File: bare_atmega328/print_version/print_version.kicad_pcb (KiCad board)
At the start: 2 copper layers, 17 parts, among them J1 22-23-2021, J2 22-23-2021, J3 640456-3, J4 22-23-2021, J5 Conn_01x14_Male, J6 Conn_01x14_Male, J7 640456-3, SW1 SW_Push, U1 ATMEGA328-PU, Y1 Crystal

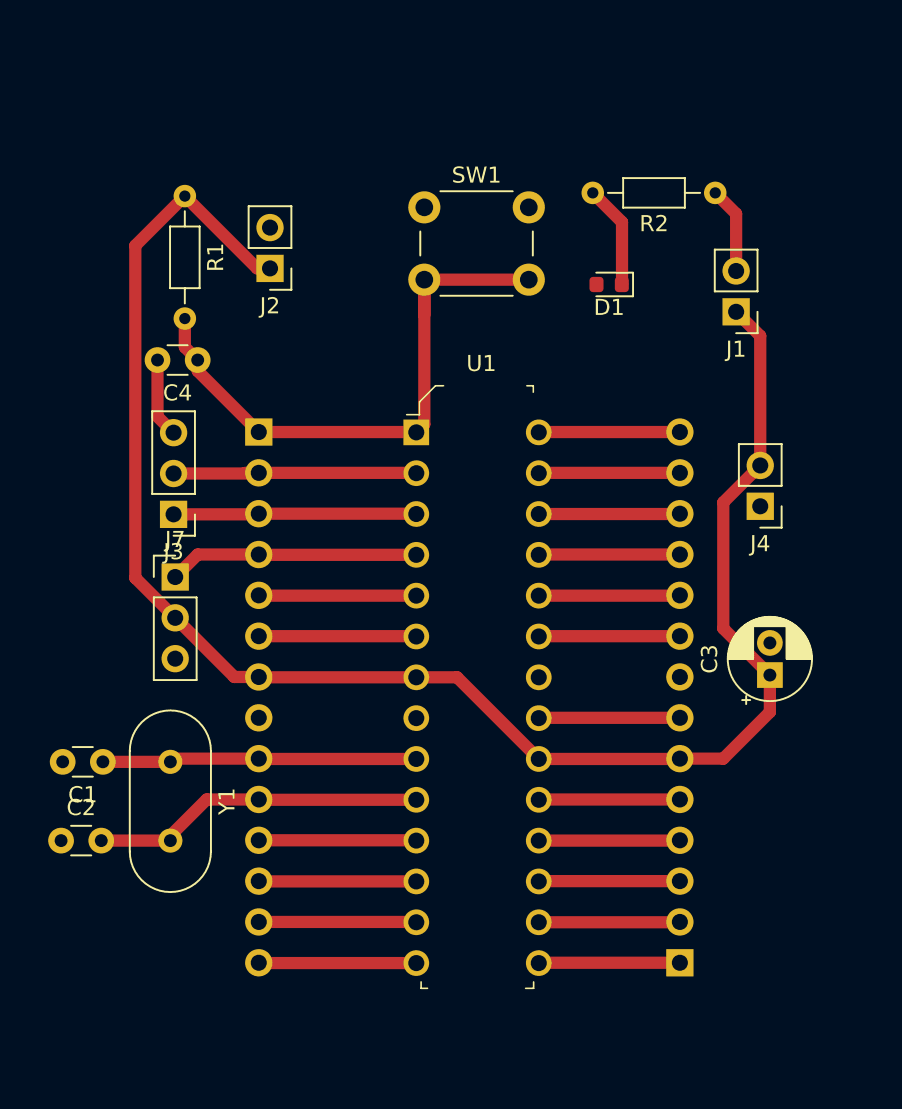
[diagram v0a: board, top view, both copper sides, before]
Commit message: Version with 555 dip
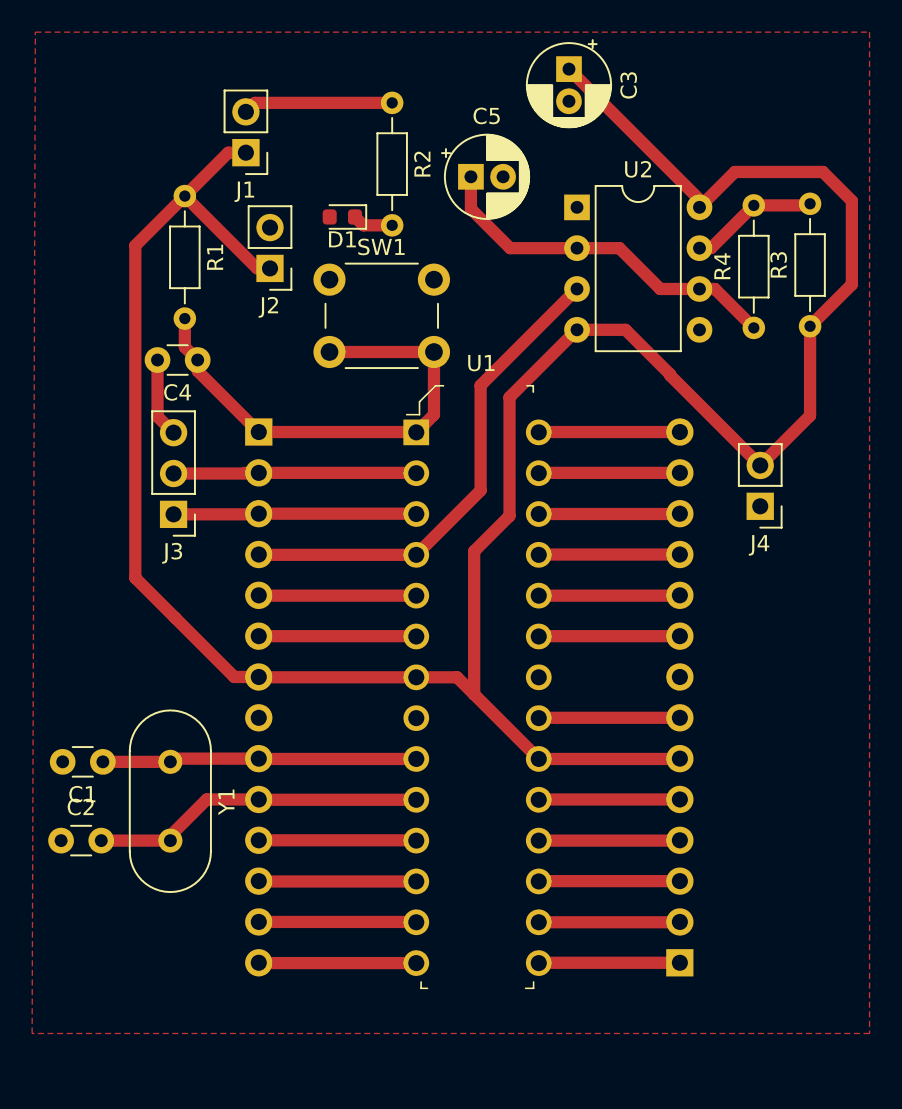
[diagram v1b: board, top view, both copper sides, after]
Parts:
- removed J7: 640456-3, Connector_PinHeader_2.54mm:PinHeader_1x03_P2.54mm_Vertical
- added C5: CP, Capacitor_THT:CP_Radial_D5.0mm_P2.00mm, F.Cu at (3.40, -15.9)
- added R3: R, Resistor_THT:R_Axial_DIN0204_L3.6mm_D1.6mm_P7.62mm_Horizontal, F.Cu at (24.5, -6.60)
- added R4: R, Resistor_THT:R_Axial_DIN0204_L3.6mm_D1.6mm_P7.62mm_Horizontal, F.Cu at (21.0, -6.50)
- added U2: NE555DR, Package_DIP:DIP-8_W7.62mm, F.Cu at (10.0, -14.0)
- moved C3 39.7 mm to (9.50, -22.6), turned to 270 degrees
- moved J1 32.1 mm to (-10.6, -17.4)
- moved R2 20.9 mm to (-1.50, -20.5), turned to 270 degrees
- moved D1 17.1 mm to (-4.60, -13.4)
- moved SW1 7.42 mm to (-5.40, -9.50)
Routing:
- net VCC: track 105.2 -> 157.9 mm
- net Net-(C5-Pad1): track 0.00 -> 22.7 mm
- net Net-(J6-Pad4): track 15.6 -> 30.5 mm
- net Net-(R3-Pad2): track 0.00 -> 8.02 mm
- net Net-(C4-Pad1): track 37.5 -> 31.7 mm
- net Net-(J1-Pad2): track 5.40 -> 9.33 mm
- net Net-(D1-Pad1): track 6.46 -> 2.53 mm
- added copper zone on F.Cu, net GND

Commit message: Version v1.2 atmega328 + 555 timer
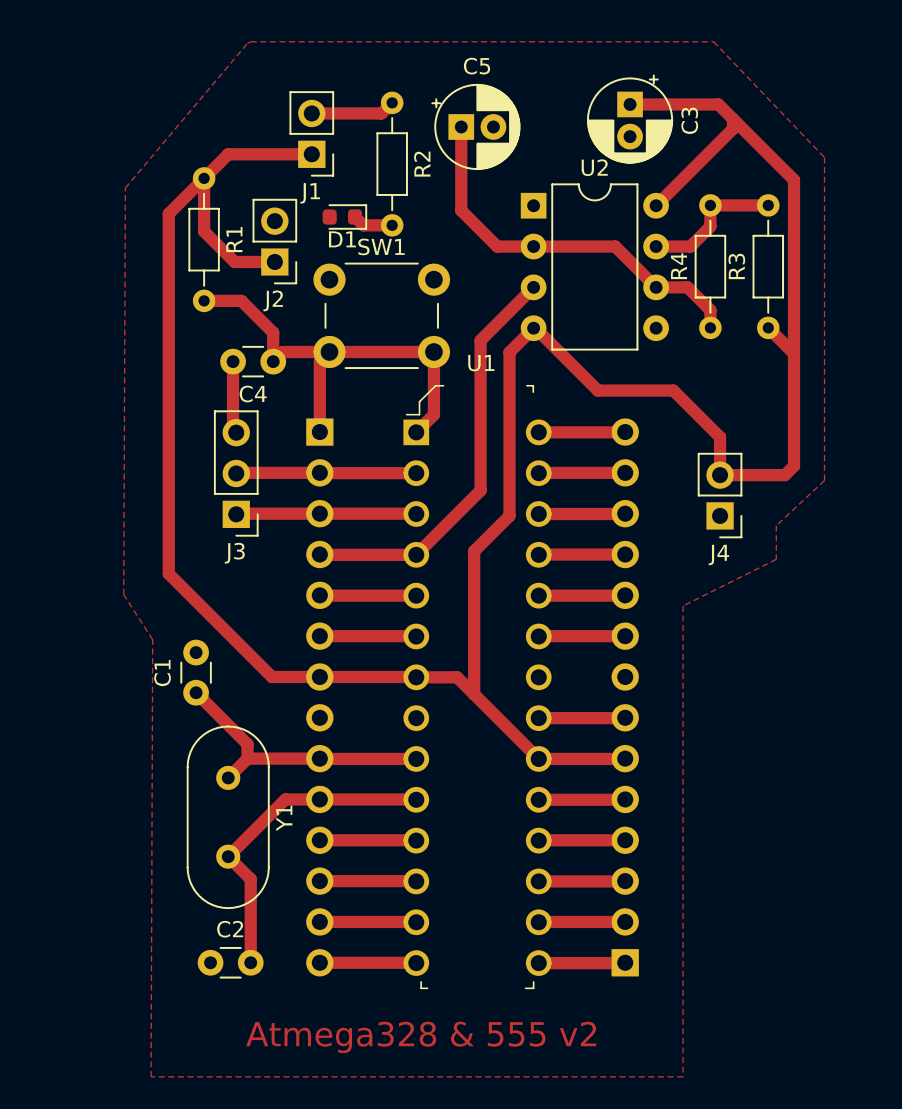
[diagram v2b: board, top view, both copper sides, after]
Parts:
- moved C2 12.0 mm to (-12.8, 33.0)
- moved C1 7.22 mm to (-13.7, 16.2), turned to 90 degrees
- moved C4 4.70 mm to (-8.90, -4.40)
- moved C3 4.39 mm to (13.3, -20.4)
- moved J1 4.10 mm to (-6.50, -17.3)
- moved J3 3.90 mm to (-11.2, 5.10)
- moved J6 3.80 mm to (-6.00, -0.02)
- moved Y1 3.74 mm to (-11.7, 21.5)
- moved J5 3.40 mm to (13.0, 33.0)
- moved C5 3.16 mm to (2.80, -19.0)
- moved U2 2.70 mm to (7.30, -14.1)
- moved R4 2.70 mm to (18.3, -6.50)
- moved R3 2.60 mm to (21.9, -6.50)
- moved J4 2.57 mm to (18.9, 5.20)
- moved R1 1.63 mm to (-13.2, -15.8)
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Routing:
- net Net-(J6-Pad4): track 30.5 -> 25.7 mm
- net Net-(J3-Pad2): track 16.0 -> 11.3 mm
- net Net-(J1-Pad2): track 9.33 -> 5.27 mm
- net Net-(J3-Pad1): track 15.1 -> 11.2 mm
- net Net-(J6-Pad5): track 9.81 -> 6.01 mm
- net Net-(J6-Pad6): track 9.81 -> 6.01 mm
- net Net-(J6-Pad14): track 9.81 -> 6.01 mm
- net Net-(J6-Pad13): track 9.81 -> 6.01 mm
- net Net-(J6-Pad12): track 9.81 -> 6.01 mm
- net Net-(J6-Pad11): track 9.81 -> 6.01 mm
- net Net-(J5-Pad9): track 8.79 -> 5.39 mm
- net Net-(J5-Pad4): track 8.79 -> 5.39 mm
- net Net-(J5-Pad2): track 8.79 -> 5.39 mm
- net Net-(J5-Pad10): track 8.79 -> 5.39 mm
- net Net-(J5-Pad13): track 8.79 -> 5.39 mm
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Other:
- board text added: "Atmega328 & 555 v2"
